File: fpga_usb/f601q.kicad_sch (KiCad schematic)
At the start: 27 parts, among them J1 Conn_01x02_Pin, U2 FT601Q, U4 AMS1117-3.3

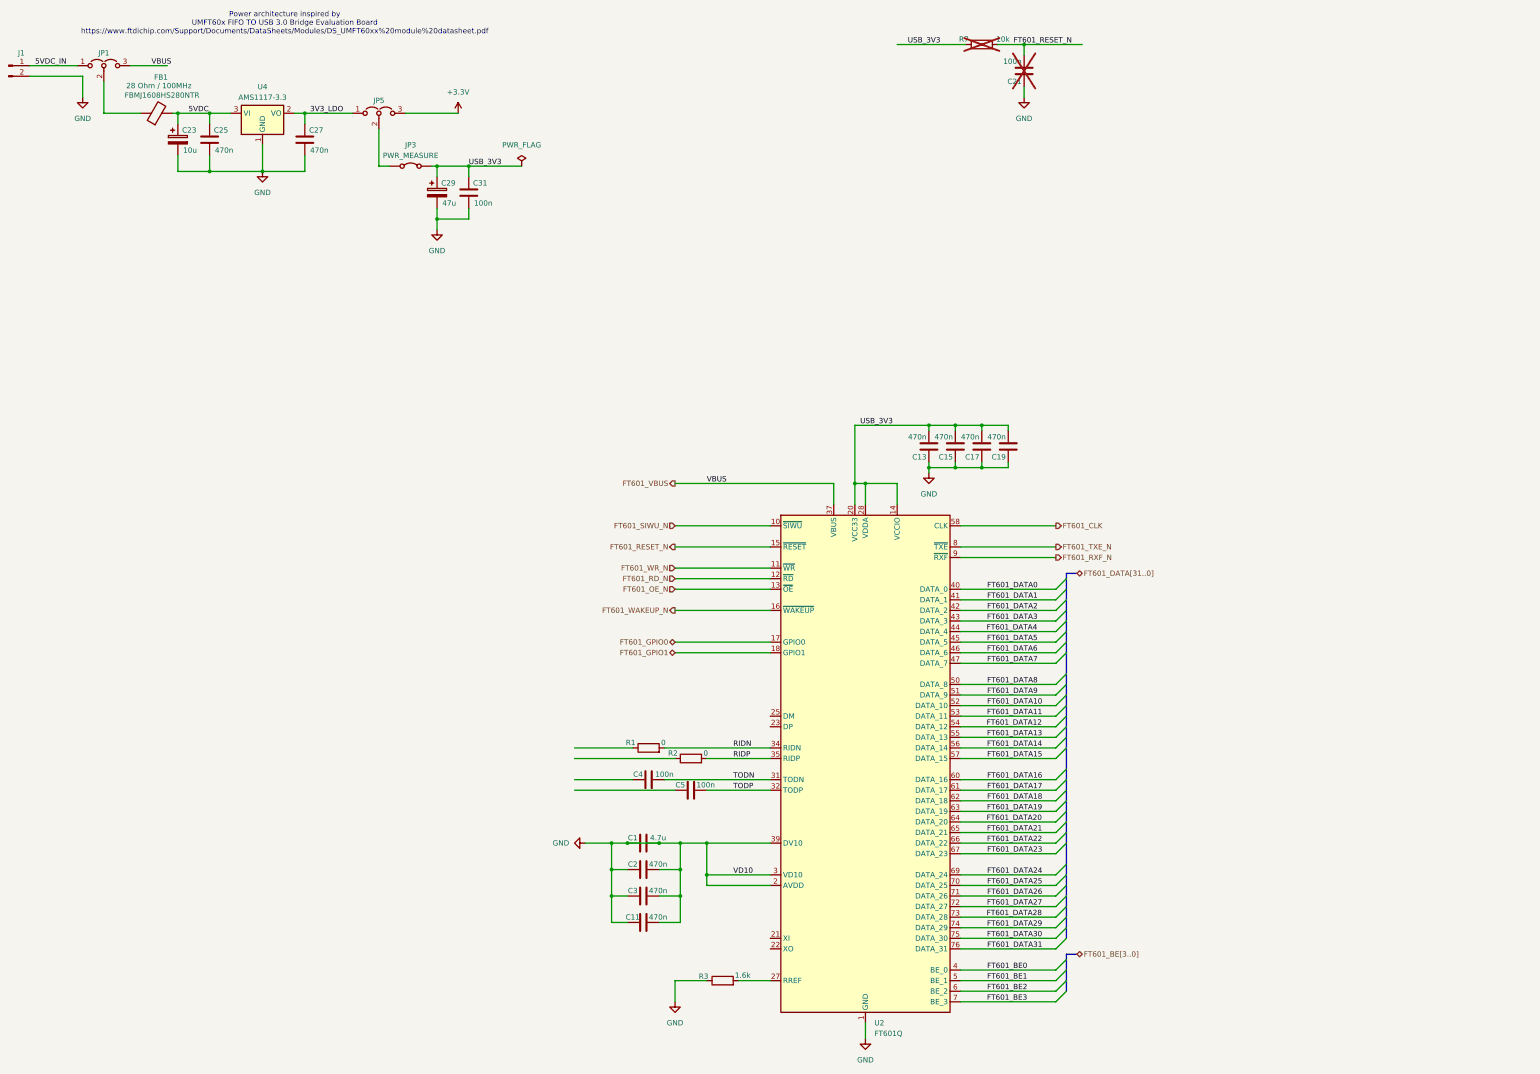
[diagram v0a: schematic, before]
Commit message: Import USB3 switch. Narrow Netclass.
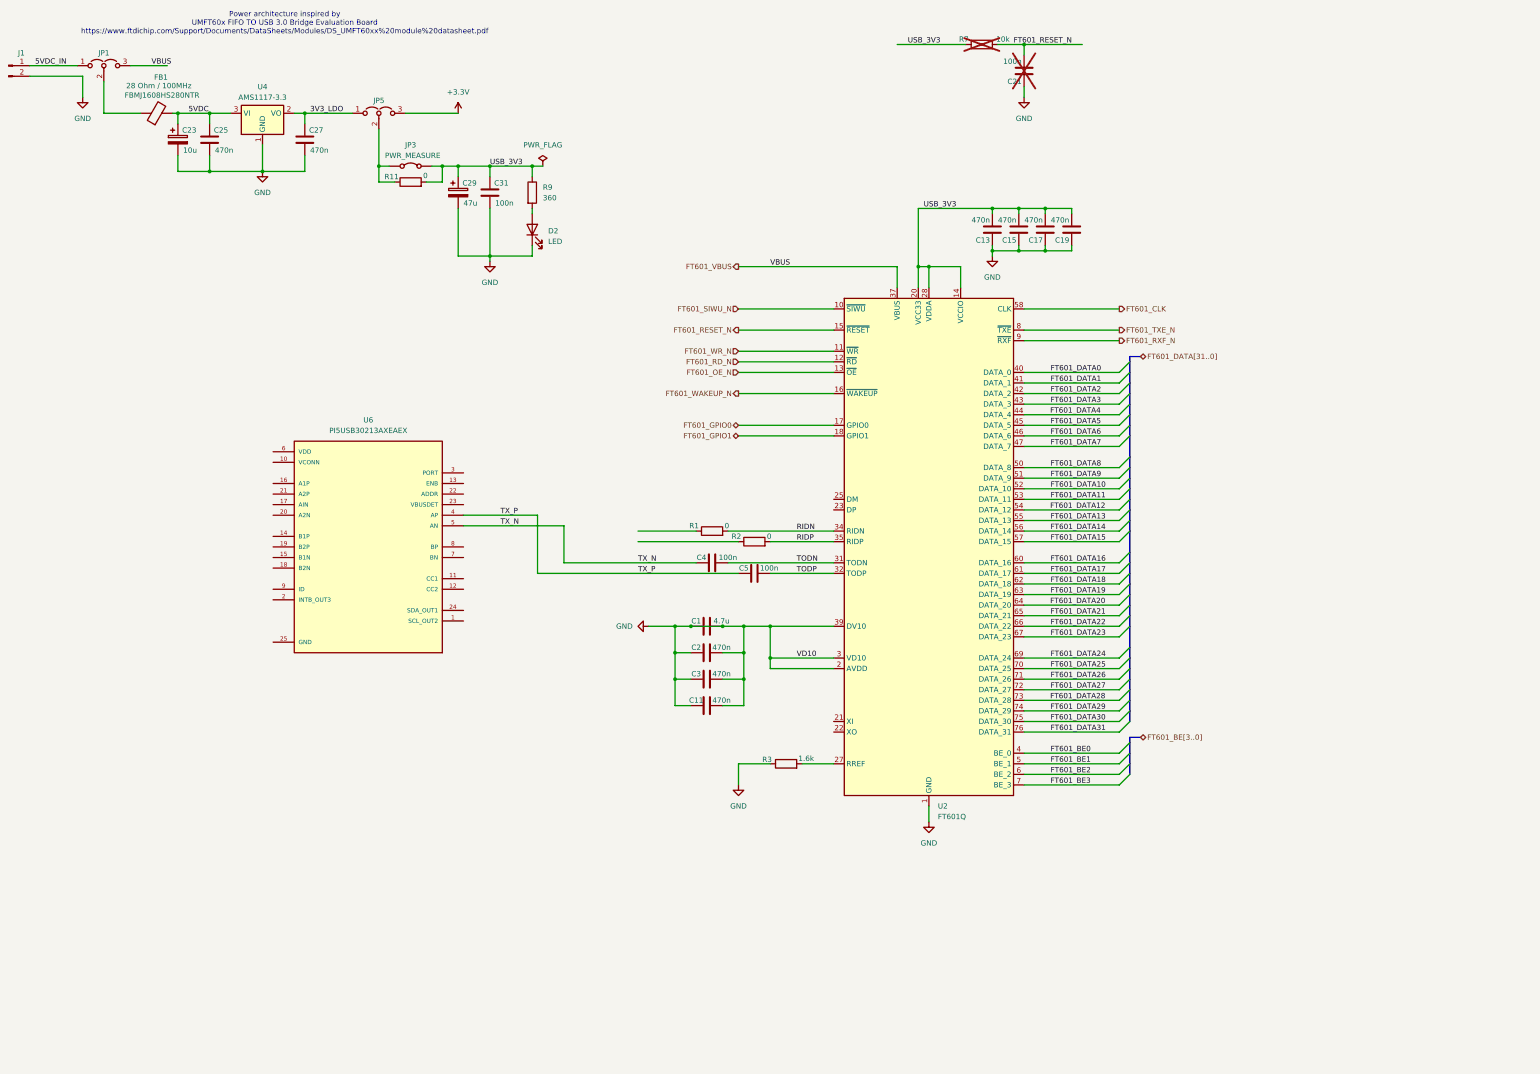
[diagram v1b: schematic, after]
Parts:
- added D2: LED, LED_SMD:LED_0805_2012Metric, symbol Device:LED
- added R11: 0, Resistor_SMD:R_0603_1608Metric, symbol Device:R
- added R9: 360, Resistor_SMD:R_0603_1608Metric, symbol Device:R
- added U6: PI5USB30213AXEAEX, PI5USB30213AXEAEX-2:QFN40P400X200X50-25N, symbol PI5USB30213AXEAEX:PI5USB30213AXEAEX
- C23: footprint (none) -> Capacitor_SMD:C_0805_2012Metric
- C25, C27, C29: footprint (none) -> Capacitor_SMD:C_0603_1608Metric
- C31: footprint (none) -> Capacitor_SMD:C_0201_0603Metric
- J1: footprint (none) -> Kicad_Personal:TerminalBlock_MAX-MX127-5.0-02P
- JP1, JP5: footprint (none) -> Connector_PinHeader_2.54mm:PinHeader_1x03_P2.54mm_Vertical
- JP3: footprint (none) -> Connector_PinHeader_2.54mm:PinHeader_1x02_P2.54mm_Vertical
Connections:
- net GND: now also D2.1 (K)
- net USB_3V3: now also R11.2, R9.1
- net TX_P: now reaches C5.1
- net TX_P: now also U6.4 (AP)
- net TX_N: now reaches C4.1
- net TX_N: now also U6.5 (AN)
- net at JP3.1 (A), JP5.2 (C): now also R11.1
- new net: D2.2 (A), R9.2
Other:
- moved on the sheet: C1, C11, C13, C15, C17, C19, C2, C29, C3, C31, C4, C5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

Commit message: First placement trial of USB0.
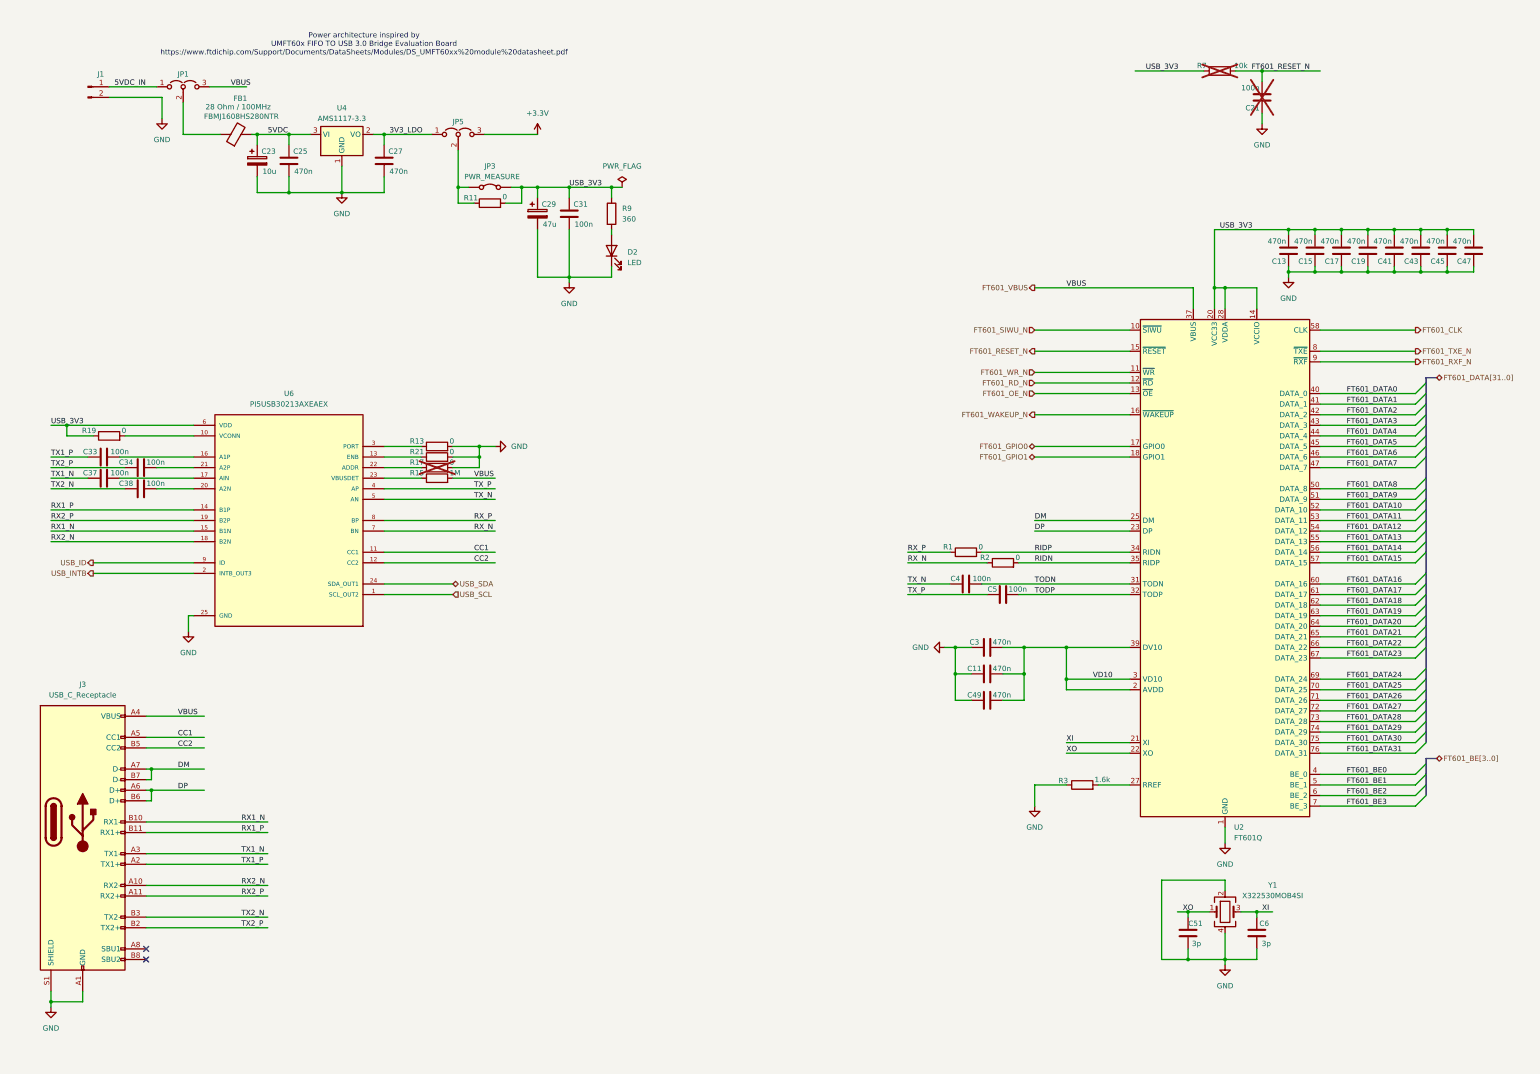
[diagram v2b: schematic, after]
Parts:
- removed C1: 4.7u, Capacitor_SMD:C_0603_1608Metric, symbol Device:C
- removed C2: 470n, Capacitor_SMD:C_0603_1608Metric, symbol Device:C
- added C33, C34, C37, C38: 100n, Capacitor_SMD:C_0402_1005Metric, symbol Device:C
- added C41, C43, C45, C47, C49: 470n, Capacitor_SMD:C_0603_1608Metric, symbol Device:C
- added C51, C6: 3p, Capacitor_SMD:C_0402_1005Metric, symbol Device:C
- added J3: USB_C_Receptacle, Connector_USB:USB_C_Receptacle_Amphenol_12401548E4-2A, symbol Connector:USB_C_Receptacle
- added R13, R17, R19, R21: 0, Resistor_SMD:R_0402_1005Metric, symbol Device:R
- added R15: 1M, Resistor_SMD:R_0402_1005Metric, symbol Device:R
- added Y1: X322530MOB4SI, Crystal:Crystal_SMD_3225-4Pin_3.2x2.5mm_HandSoldering, symbol Device:Crystal_GND24
- C31: footprint Capacitor_SMD:C_0201_0603Metric -> Capacitor_SMD:C_0402_1005Metric
- C4, C5: footprint Capacitor_SMD:C_0603_1608Metric -> Capacitor_SMD:C_0402_1005Metric
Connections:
- net FT601_VBUS: now also J3.A4 (VBUS), J3.A9 (VBUS), J3.B4 (VBUS), J3.B9 (VBUS), R15.2
- net GND: now also U6.25 (GND), C41.1, C43.1, C45.1, C47.1, C49.1, C51.1, C6.1, J3.A1 (GND), J3.A12 (GND), J3.B1 (GND), J3.B12 (GND), J3.S1 (SHIELD), R13.2, R17.2, R21.2, Y1.2, Y1.4; no longer C11.2, C3.2, U2.2 (AVDD), U2.3 (VD10), U2.30 (VD10), U2.33 (VD10), U2.39 (DV10), U2.48 (VD10)
- net RIDN: now also R2.2, U2.35 (RIDP); no longer R1.2, U2.34 (RIDN)
- net RIDP: now also R1.2, U2.34 (RIDN); no longer R2.2, U2.35 (RIDP)
- net USB_3V3: now also U6.6 (VDD), C41.2, C43.2, C45.2, C47.2, R19.1
- net XI: now reaches U2.21 (XI)
- net XI: now also C6.2, Y1.3
- net XO: now reaches U2.22 (XO)
- net XO: now also C51.2, Y1.1
- net DP: now reaches U2.23 (DP)
- net DP: now also J3.A6 (D+), J3.B6 (D+)
- net DM: now reaches U2.25 (DM)
- net DM: now also J3.A7 (D-), J3.B7 (D-)
- net USB_SCL: now reaches U6.1 (SCL_OUT2)
- net at U6.10 (VCONN): now also R19.2
- net CC1: now reaches U6.11 (CC1)
- net CC1: now also J3.A5 (CC1)
- net CC2: now reaches U6.12 (CC2)
- net CC2: now also J3.B5 (CC2)
- net at U6.13 (ENB): now also R21.1
- net RX1_P: now reaches U6.14 (B1P)
- net RX1_P: now also J3.B11 (RX1+)
- net RX1_N: now reaches U6.15 (B1N)
- net RX1_N: now also J3.B10 (RX1-)
- net at U6.16 (A1P): now also C33.2
- net at U6.17 (AIN): now also C37.2
- net RX2_N: now reaches U6.18 (B2N)
- net RX2_N: now also J3.A10 (RX2-)
- net RX2_P: now reaches U6.19 (B2P)
- net RX2_P: now also J3.A11 (RX2+)
- net USB_INTB: now reaches U6.2 (INTB_OUT3)
- net at U6.20 (A2N): now also C38.2
- net at U6.21 (A2P): now also C34.2
- net at U6.22 (ADDR): now also R17.1
- net at U6.23 (VBUSDET): now also R15.1
- net USB_SDA: now reaches U6.24 (SDA_OUT1)
- net at U6.3 (PORT): now also R13.1
- net RX_N: now reaches U6.7 (BN)
- net RX_N: now also R2.1
- net RX_P: now reaches U6.8 (BP)
- net RX_P: now also R1.1
- net USB_ID: now reaches U6.9 (ID)
- new net TX1_N: C37.1, J3.A3 (TX1-)
- new net TX1_P: C33.1, J3.A2 (TX1+)
- new net TX2_N: C38.1, J3.B3 (TX2-)
- new net TX2_P: C34.1, J3.B2 (TX2+)
- new net VD10: C11.2, C3.2, C49.2, U2.2 (AVDD), U2.3 (VD10), U2.30 (VD10), U2.33 (VD10), U2.39 (DV10), U2.48 (VD10)
- no-connect marks 0 -> 2
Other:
- moved on the sheet: C13, C15, C17, C19, C21, C23, C25, C27, C29, C3, C31, C4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
